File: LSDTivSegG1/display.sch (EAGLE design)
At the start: 96 parts, among them IC1 MEGA8-P, IC2 MAX232, IC3 PCF8574P, IC4 PCF8574P, IC5 PCF8574P, IC6 PCF8574P

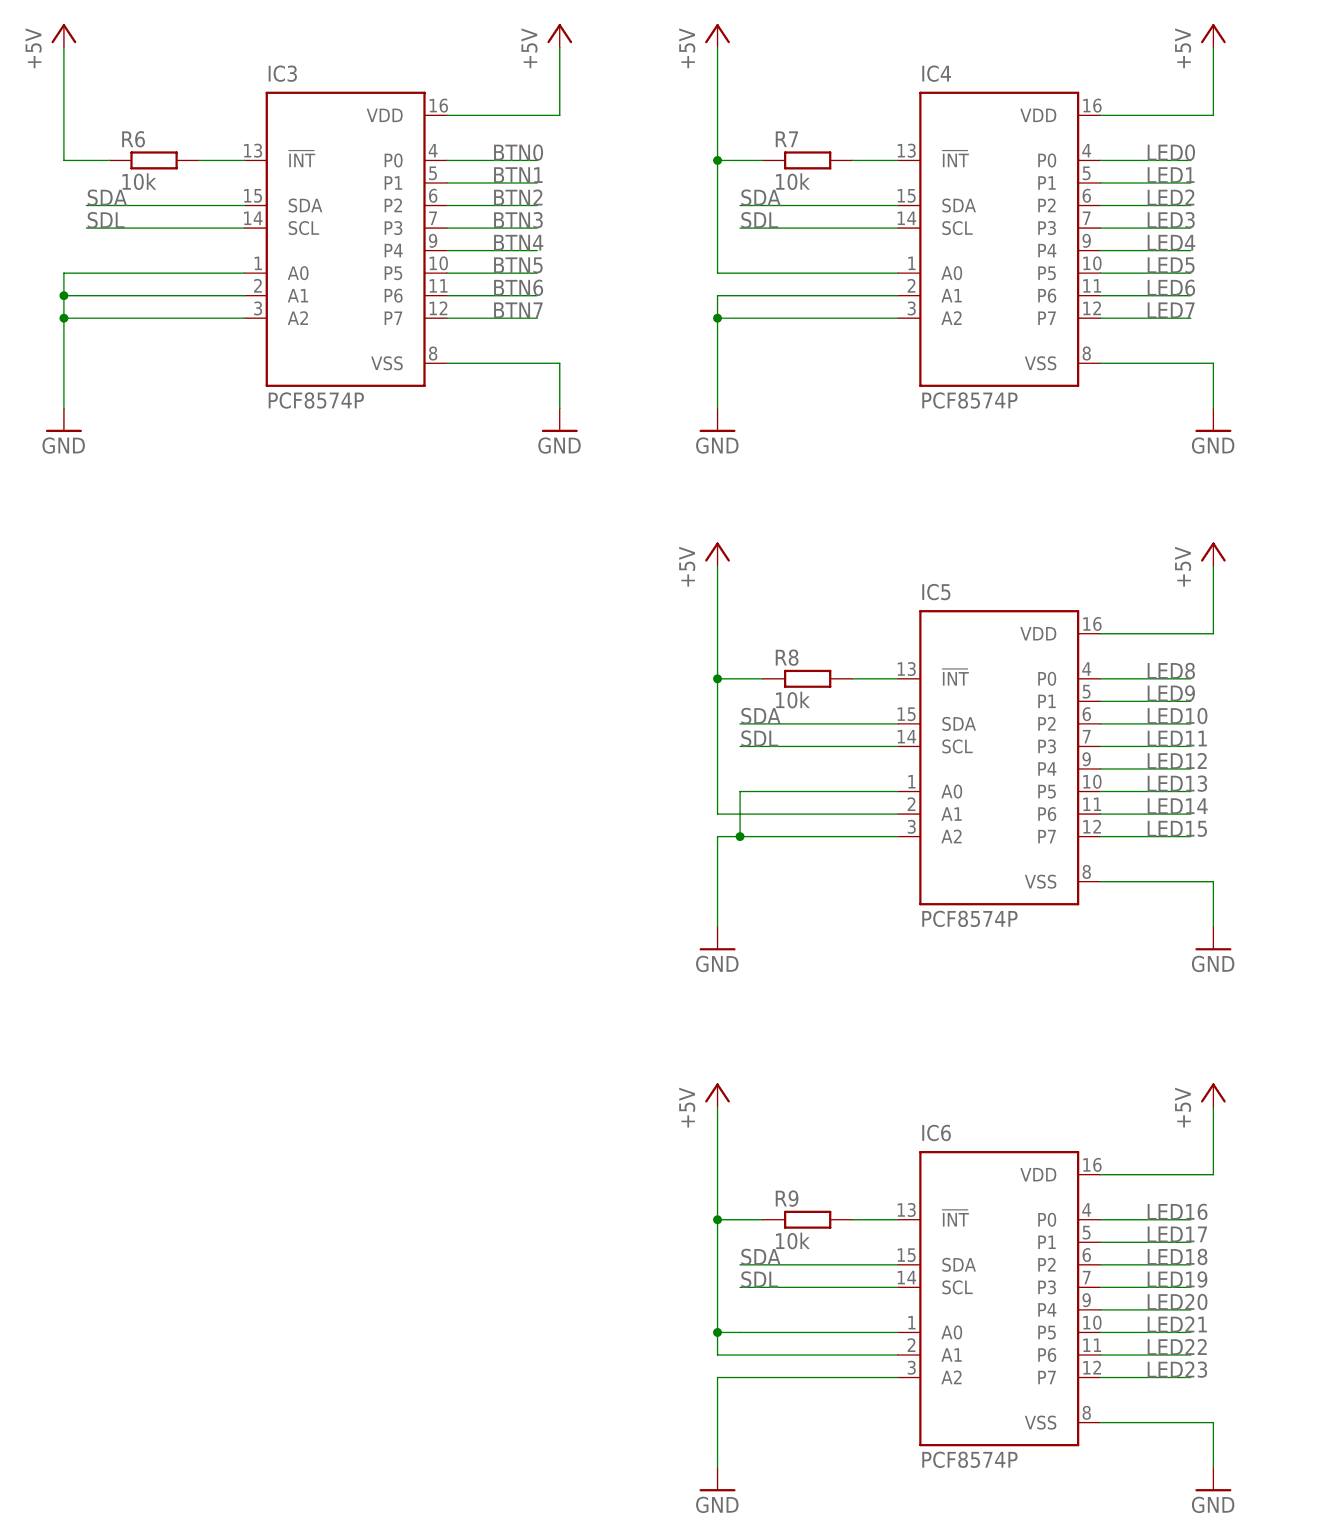
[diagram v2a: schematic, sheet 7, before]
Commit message: added blocking capacities to IO-Expanders
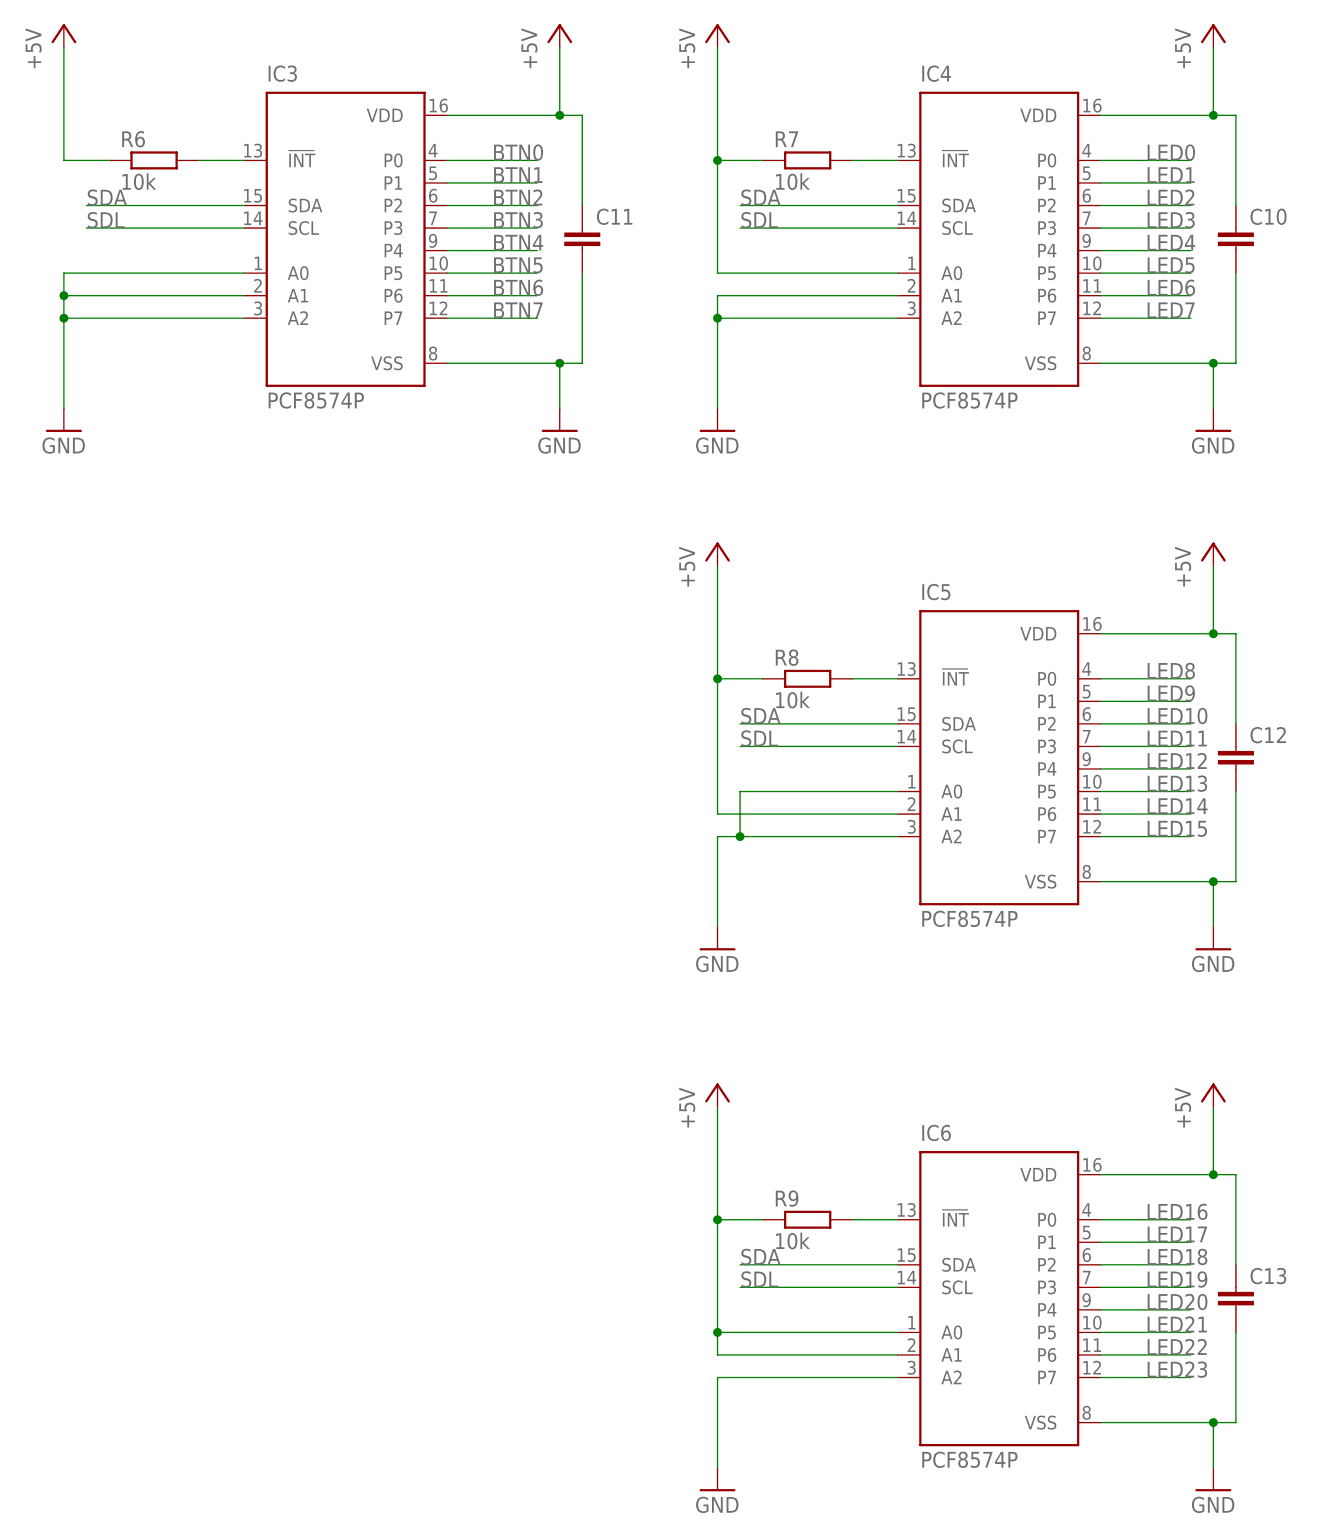
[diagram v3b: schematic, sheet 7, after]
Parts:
- added C10, C11, C12, C13: (no value), rcl:C-EU025-025X050
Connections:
- net +5V: now also C10.1, C11.1, C12.1, C13.1
- net GND: now also C10.2, C11.2, C12.2, C13.2
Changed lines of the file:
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@@
 <part name="JP1" library="pinhead" library_urn="urn:adsk.eagle:library:325" deviceset="PINHD-1X2" device="" package3d_urn="urn:adsk.eagle:package:22435/2"/>
 <part name="JP2" library="pinhead" library_urn="urn:adsk.eagle:library:325" deviceset="PINHD-2X3" device="" package3d_urn="urn:adsk.eagle:package:22462/2"/>
+<part name="C10" library="rcl" library_urn="urn:adsk.eagle:library:334" deviceset="C-EU" device="025-025X050" package3d_urn="urn:adsk.eagle:package:23629/2"/>
+<part name="C11" library="rcl" library_urn="urn:adsk.eagle:library:334" deviceset="C-EU" device="025-025X050" package3d_urn="urn:adsk.eagle:package:23629/2"/>
+<part name="C12" library="rcl" library_urn="urn:adsk.eagle:library:334" deviceset="C-EU" device="025-025X050" package3d_urn="urn:adsk.eagle:package:23629/2"/>
+<part name="C13" library="rcl" library_urn="urn:adsk.eagle:library:334" deviceset="C-EU" device="025-025X050" package3d_urn="urn:adsk.eagle:package:23629/2"/>
 </parts>
 <sheets>
@@
 <instance part="GND16" gate="1" x="50.8" y="-124.46"/>
 <instance part="FRAME7" gate="G$1" x="-45.72" y="-172.72"/>
+<instance part="C10" gate="G$1" x="109.22" y="17.78"/>
+<instance part="C11" gate="G$1" x="35.56" y="17.78"/>
+<instance part="C12" gate="G$1" x="109.22" y="-40.64"/>
+<instance part="C13" gate="G$1" x="109.22" y="-101.6"/>
 </instances>
 <busses>
@@
 <wire x1="20.32" y1="30.48" x2="33.02" y2="30.48" width="0.1524" layer="91"/>
 <wire x1="33.02" y1="30.48" x2="33.02" y2="38.1" width="0.1524" layer="91"/>
+<pinref part="C11" gate="G$1" pin="1"/>
+<wire x1="33.02" y1="30.48" x2="35.56" y2="30.48" width="0.1524" layer="91"/>
+<wire x1="35.56" y1="30.48" x2="35.56" y2="20.32" width="0.1524" layer="91"/>
+<junction x="33.02" y="30.48"/>
 </segment>
 <segment>
@@
 <wire x1="93.98" y1="30.48" x2="106.68" y2="30.48" width="0.1524" layer="91"/>
 <wire x1="106.68" y1="30.48" x2="106.68" y2="38.1" width="0.1524" layer="91"/>
+<pinref part="C10" gate="G$1" pin="1"/>
+<wire x1="106.68" y1="30.48" x2="109.22" y2="30.48" width="0.1524" layer="91"/>
+<wire x1="109.22" y1="30.48" x2="109.22" y2="20.32" width="0.1524" layer="91"/>
+<junction x="106.68" y="30.48"/>
 </segment>
 <segment>
@@
 <wire x1="93.98" y1="-27.94" x2="106.68" y2="-27.94" width="0.1524" layer="91"/>
 <wire x1="106.68" y1="-27.94" x2="106.68" y2="-20.32" width="0.1524" layer="91"/>
+<pinref part="C12" gate="G$1" pin="1"/>
+<wire x1="106.68" y1="-27.94" x2="109.22" y2="-27.94" width="0.1524" layer="91"/>
+<wire x1="109.22" y1="-27.94" x2="109.22" y2="-38.1" width="0.1524" layer="91"/>
+<junction x="106.68" y="-27.94"/>
 </segment>
 <segment>
@@
 <wire x1="93.98" y1="-88.9" x2="106.68" y2="-88.9" width="0.1524" layer="91"/>
 <wire x1="106.68" y1="-88.9" x2="106.68" y2="-81.28" width="0.1524" layer="91"/>
+<pinref part="C13" gate="G$1" pin="1"/>
+<wire x1="106.68" y1="-88.9" x2="109.22" y2="-88.9" width="0.1524" layer="91"/>
+<wire x1="109.22" y1="-88.9" x2="109.22" y2="-99.06" width="0.1524" layer="91"/>
+<junction x="106.68" y="-88.9"/>
 </segment>
 <segment>
@@
 <wire x1="20.32" y1="2.54" x2="33.02" y2="2.54" width="0.1524" layer="91"/>
 <wire x1="33.02" y1="2.54" x2="33.02" y2="-2.54" width="0.1524" layer="91"/>
+<pinref part="C11" gate="G$1" pin="2"/>
+<wire x1="35.56" y1="12.7" x2="35.56" y2="2.54" width="0.1524" layer="91"/>
+<wire x1="35.56" y1="2.54" x2="33.02" y2="2.54" width="0.1524" layer="91"/>
+<junction x="33.02" y="2.54"/>
 </segment>
 <segment>
@@
 <wire x1="93.98" y1="2.54" x2="106.68" y2="2.54" width="0.1524" layer="91"/>
 <wire x1="106.68" y1="2.54" x2="106.68" y2="-2.54" width="0.1524" layer="91"/>
+<pinref part="C10" gate="G$1" pin="2"/>
+<wire x1="109.22" y1="12.7" x2="109.22" y2="2.54" width="0.1524" layer="91"/>
+<wire x1="109.22" y1="2.54" x2="106.68" y2="2.54" width="0.1524" layer="91"/>
+<junction x="106.68" y="2.54"/>
 </segment>
 <segment>
@@
 <wire x1="93.98" y1="-55.88" x2="106.68" y2="-55.88" width="0.1524" layer="91"/>
 <wire x1="106.68" y1="-55.88" x2="106.68" y2="-60.96" width="0.1524" layer="91"/>
+<pinref part="C12" gate="G$1" pin="2"/>
+<wire x1="109.22" y1="-45.72" x2="109.22" y2="-55.88" width="0.1524" layer="91"/>
+<wire x1="109.22" y1="-55.88" x2="106.68" y2="-55.88" width="0.1524" layer="91"/>
+<junction x="106.68" y="-55.88"/>
 </segment>
 <segment>
@@
 <wire x1="93.98" y1="-116.84" x2="106.68" y2="-116.84" width="0.1524" layer="91"/>
 <wire x1="106.68" y1="-116.84" x2="106.68" y2="-121.92" width="0.1524" layer="91"/>
-</segment>
-<segment>
+<pinref part="C13" gate="G$1" pin="2"/>
+<wire x1="109.22" y1="-106.68" x2="109.22" y2="-116.84" width="0.1524" layer="91"/>
+<wire x1="109.22" y1="-116.84" x2="106.68" y2="-116.84" width="0.1524" layer="91"/>
+<junction x="106.68" y="-116.84"/>
+</segment>
+<segment>

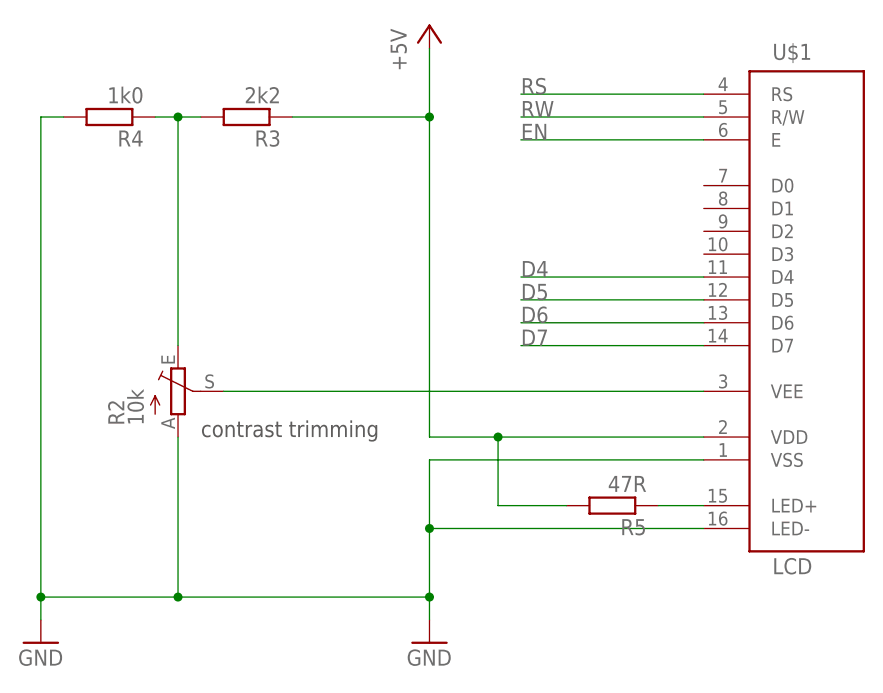
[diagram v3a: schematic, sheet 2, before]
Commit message: updated display contrast trimming circuit
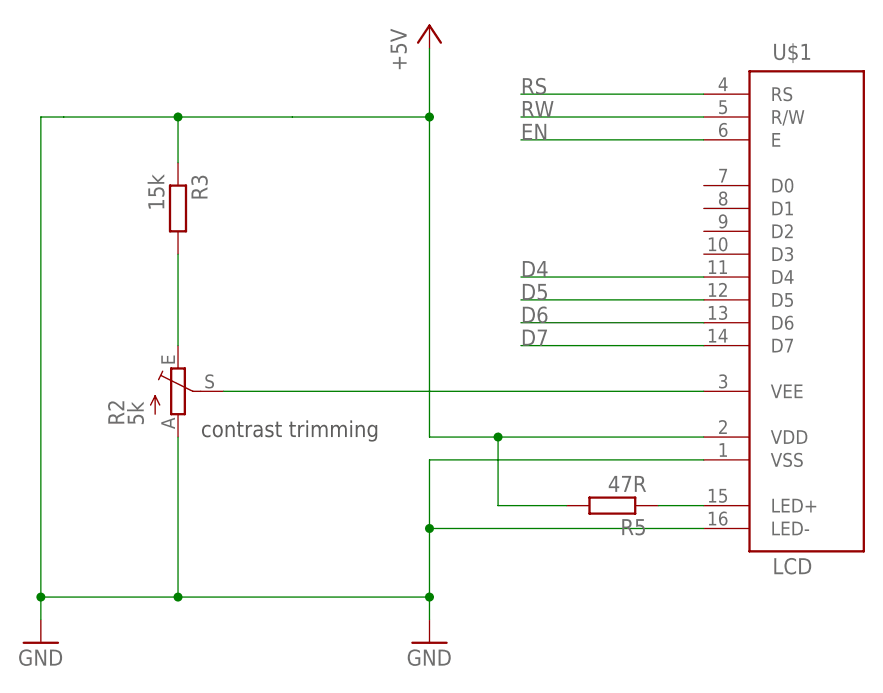
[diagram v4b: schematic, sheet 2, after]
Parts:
- removed R4: 1k0, rcl:R-EU_0207/10
- R2: value 10k -> 5k
- R3: value 2k2 -> 15k
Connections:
- net +5V: now also R2.A, U$1.LED-, U$1.VSS
- net GND: no longer R2.A, R4.2, U$1.LED-, U$1.VSS
- net N$9: no longer R4.1
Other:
- moved on the sheet: R3
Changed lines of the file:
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@@
 <part name="P+5" library="hcontrol" deviceset="+5V" device=""/>
 <part name="GND7" library="SparkFun-Aesthetics" deviceset="GND" device=""/>
-<part name="R2" library="pot" library_urn="urn:adsk.eagle:library:331" deviceset="TRIM_EU-" device="PT10" package3d_urn="urn:adsk.eagle:package:22715/1" value="10k"/>
-<part name="R3" library="rcl" library_urn="urn:adsk.eagle:library:334" deviceset="R-EU_" device="0207/10" package3d_urn="urn:adsk.eagle:package:23491/1" value="2k2"/>
-<part name="R4" library="rcl" library_urn="urn:adsk.eagle:library:334" deviceset="R-EU_" device="0207/10" package3d_urn="urn:adsk.eagle:package:23491/1" value="1k0"/>
+<part name="R2" library="pot" library_urn="urn:adsk.eagle:library:331" deviceset="TRIM_EU-" device="PT10" package3d_urn="urn:adsk.eagle:package:22715/1" value="5k"/>
 <part name="GND8" library="SparkFun-Aesthetics" deviceset="GND" device=""/>
 <part name="R5" library="rcl" library_urn="urn:adsk.eagle:library:334" deviceset="R-EU_" device="0207/10" package3d_urn="urn:adsk.eagle:package:23491/1" value="47R"/>
@@
 <part name="C12" library="rcl" library_urn="urn:adsk.eagle:library:334" deviceset="C-EU" device="025-025X050" package3d_urn="urn:adsk.eagle:package:23629/2"/>
 <part name="C13" library="rcl" library_urn="urn:adsk.eagle:library:334" deviceset="C-EU" device="025-025X050" package3d_urn="urn:adsk.eagle:package:23629/2"/>
+<part name="R3" library="rcl" library_urn="urn:adsk.eagle:library:334" deviceset="R-EU_" device="0207/10" package3d_urn="urn:adsk.eagle:package:23491/1" value="15k"/>
 </parts>
 <sheets>
@@
 <instance part="GND7" gate="1" x="-35.56" y="-10.16"/>
 <instance part="R2" gate="1" x="-63.5" y="17.78"/>
-<instance part="R3" gate="G$1" x="-55.88" y="48.26" rot="R180"/>
-<instance part="R4" gate="G$1" x="-71.12" y="48.26" rot="R180"/>
 <instance part="GND8" gate="1" x="-78.74" y="-10.16"/>
 <instance part="R5" gate="G$1" x="-15.24" y="5.08" rot="R180"/>
 <instance part="FRAME2" gate="G$1" x="-165.1" y="-71.12"/>
+<instance part="R3" gate="G$1" x="-63.5" y="38.1" rot="R270"/>
 </instances>
 <busses>
@@
 <wire x1="-50.8" y1="48.26" x2="-35.56" y2="48.26" width="0.1524" layer="91"/>
 <junction x="-35.56" y="48.26"/>
-<pinref part="R3" gate="G$1" pin="1"/>
 <pinref part="R5" gate="G$1" pin="2"/>
 <wire x1="-20.32" y1="5.08" x2="-27.94" y2="5.08" width="0.1524" layer="91"/>
 <wire x1="-27.94" y1="5.08" x2="-27.94" y2="12.7" width="0.1524" layer="91"/>
 <junction x="-27.94" y="12.7"/>
-</segment>
-</net>
-<net name="GND" class="0">
-<segment>
-<pinref part="R4" gate="G$1" pin="2"/>
 <wire x1="-76.2" y1="48.26" x2="-78.74" y2="48.26" width="0.1524" layer="91"/>
 <wire x1="-78.74" y1="48.26" x2="-78.74" y2="-5.08" width="0.1524" layer="91"/>
@@
 <wire x1="-5.08" y1="2.54" x2="-35.56" y2="2.54" width="0.1524" layer="91"/>
 <junction x="-35.56" y="2.54"/>
-</segment>
-</net>
-<net name="N$9" class="0">
-<segment>
-<pinref part="R3" gate="G$1" pin="2"/>
-<pinref part="R4" gate="G$1" pin="1"/>
-<wire x1="-60.96" y1="48.26" x2="-63.5" y2="48.26" width="0.1524" layer="91"/>
-<pinref part="R2" gate="1" pin="E"/>
-<wire x1="-63.5" y1="48.26" x2="-66.04" y2="48.26" width="0.1524" layer="91"/>
-<wire x1="-63.5" y1="22.86" x2="-63.5" y2="48.26" width="0.1524" layer="91"/>
+<pinref part="R3" gate="G$1" pin="1"/>
+<wire x1="-76.2" y1="48.26" x2="-63.5" y2="48.26" width="0.1524" layer="91"/>
+<wire x1="-63.5" y1="48.26" x2="-63.5" y2="43.18" width="0.1524" layer="91"/>
+<wire x1="-50.8" y1="48.26" x2="-63.5" y2="48.26" width="0.1524" layer="91"/>
 <junction x="-63.5" y="48.26"/>
 </segment>
@@
 </segment>
 </net>
+<net name="N$9" class="0">
+<segment>
+<pinref part="R2" gate="1" pin="E"/>
+<pinref part="R3" gate="G$1" pin="2"/>
+<wire x1="-63.5" y1="22.86" x2="-63.5" y2="33.02" width="0.1524" layer="91"/>
+</segment>
+</net>

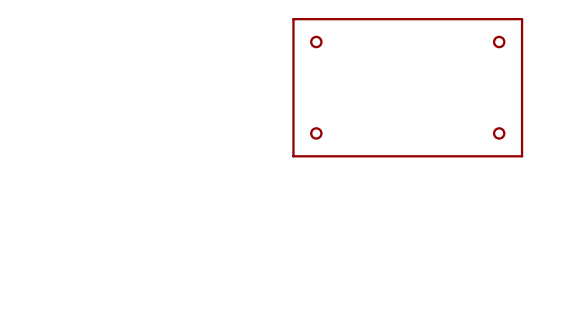
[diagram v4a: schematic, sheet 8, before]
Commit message: added display board frame to library replaced board frame in display schematic
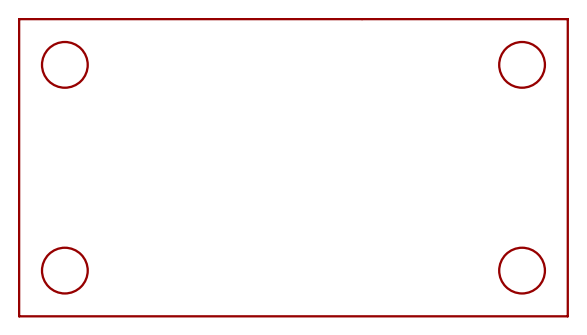
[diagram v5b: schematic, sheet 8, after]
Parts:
- U$2: value PCB -> DISPLAY_FRAME; device lsd2016:PCB -> lsd2016:DISPLAY_FRAME
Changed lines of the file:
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@@
 <part name="R39" library="rcl" library_urn="urn:adsk.eagle:library:334" deviceset="R-EU_" device="0207/10" package3d_urn="urn:adsk.eagle:package:23491/1" value="150R"/>
 <part name="GND2" library="SparkFun-Aesthetics" deviceset="GND" device=""/>
-<part name="U$2" library="lsd2016" deviceset="PCB" device=""/>
 <part name="FRAME1" library="frames" library_urn="urn:adsk.eagle:library:229" deviceset="A4L-LOC" device=""/>
 <part name="FRAME2" library="frames" library_urn="urn:adsk.eagle:library:229" deviceset="A4L-LOC" device=""/>
@@
 <part name="C13" library="rcl" library_urn="urn:adsk.eagle:library:334" deviceset="C-EU" device="025-025X050" package3d_urn="urn:adsk.eagle:package:23629/2"/>
 <part name="R3" library="rcl" library_urn="urn:adsk.eagle:library:334" deviceset="R-EU_" device="0207/10" package3d_urn="urn:adsk.eagle:package:23491/1" value="15k"/>
+<part name="U$2" library="lsd2016" deviceset="DISPLAY_FRAME" device=""/>
 </parts>
 <sheets>
@@
 </plain>
 <instances>
-<instance part="U$2" gate="G$1" x="12.7" y="7.62"/>
+<instance part="U$2" gate="G$1" x="15.24" y="0"/>
 </instances>
 <busses>
